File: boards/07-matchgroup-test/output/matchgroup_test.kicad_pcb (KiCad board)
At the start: 4 copper layers, 110 x 95 mm, 8 parts, among them J1 FFC6_MIPI, J2 HDMI19, J3 ADDR_HDR, U1 QFN48_DDR_CTRL, U2 QFN48_DRAM, U3 QFN24_MIPI, U4 BGA49_HDMI, U5 QFP48_SRAM

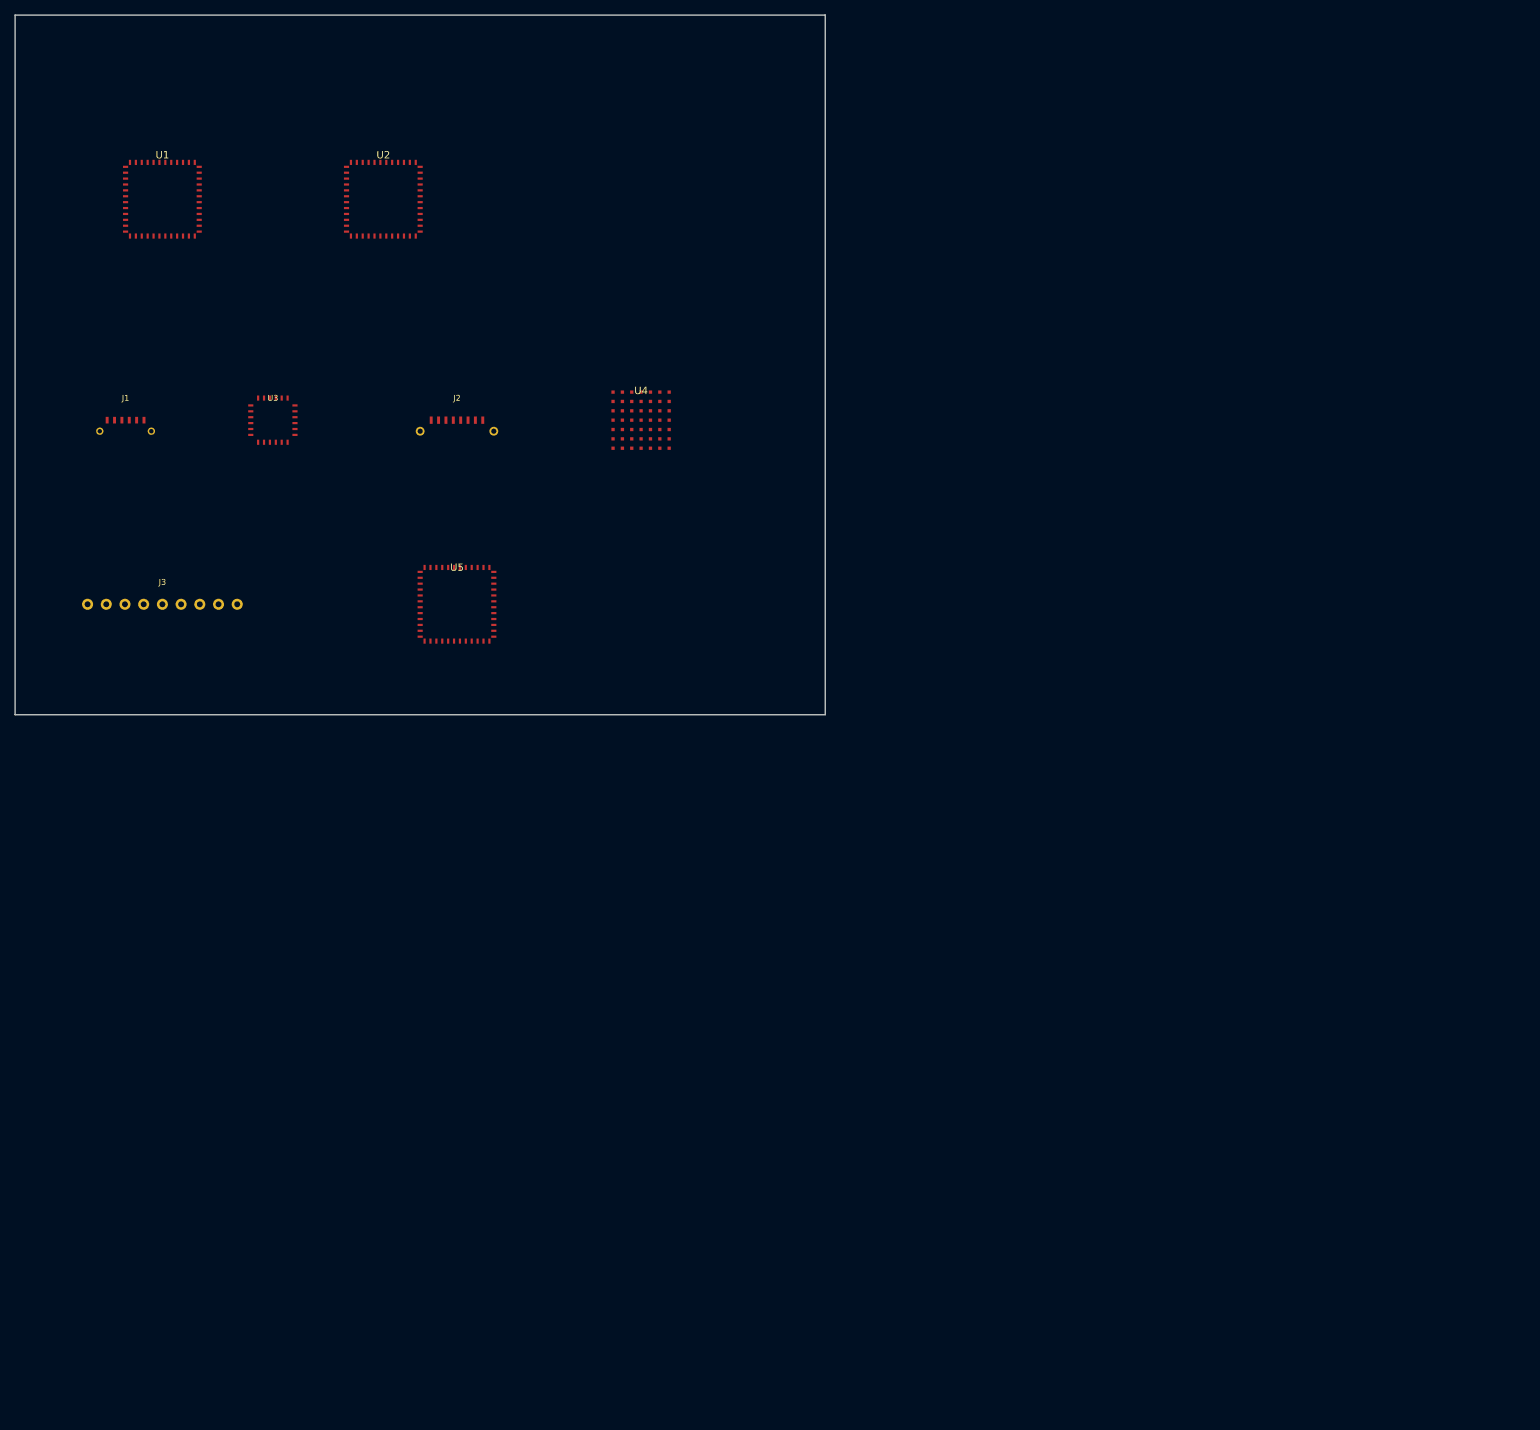
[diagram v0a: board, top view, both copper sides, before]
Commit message: fix(pcb): page-fit routed boards only; revert unrouted sources (refs #3714)
page_fit was applied to and committed for the UNROUTED board sources too.
Because the autorouter is absolute-grid-position-dependent, translating the
unrouted boards changed routing outcomes and turned CI red on three jobs:
- Test: board-02 re-route produced a platform-specific segment count.
- Diff-Pair (06) / Match-Group (07): re-routing the moved unrouted boards
  fractured plane nets under the copper-union pour audit (#3509/#3617).

page_fit is a pure post-route translation, so it must touch the ROUTED
output only:
- Revert every unrouted boards/*/output/<name>.kicad_pcb to origin/main
  (byte-identical); keep the page-fitted *_routed.kicad_pcb (gallery/viewer).
- Revert tests/router/test_board02_manufacturable_baseline.py to main
  (unrouted board-02 unchanged -> reproduces main's result).
- Build hook: _run_step_page_fit now operates on the routed PCB only and
  skips cleanly when no routed output exists, instead of falling back to and
  persisting a page-fit unrouted PCB.

Retains the sound geometry fixes (translation-invariant
point_to_segment_distance, _format_coord_mm, diffpair +1e-6 window tolerance).

Co-Authored-By: Claude Opus 4.7 <noreply@anthropic.com>
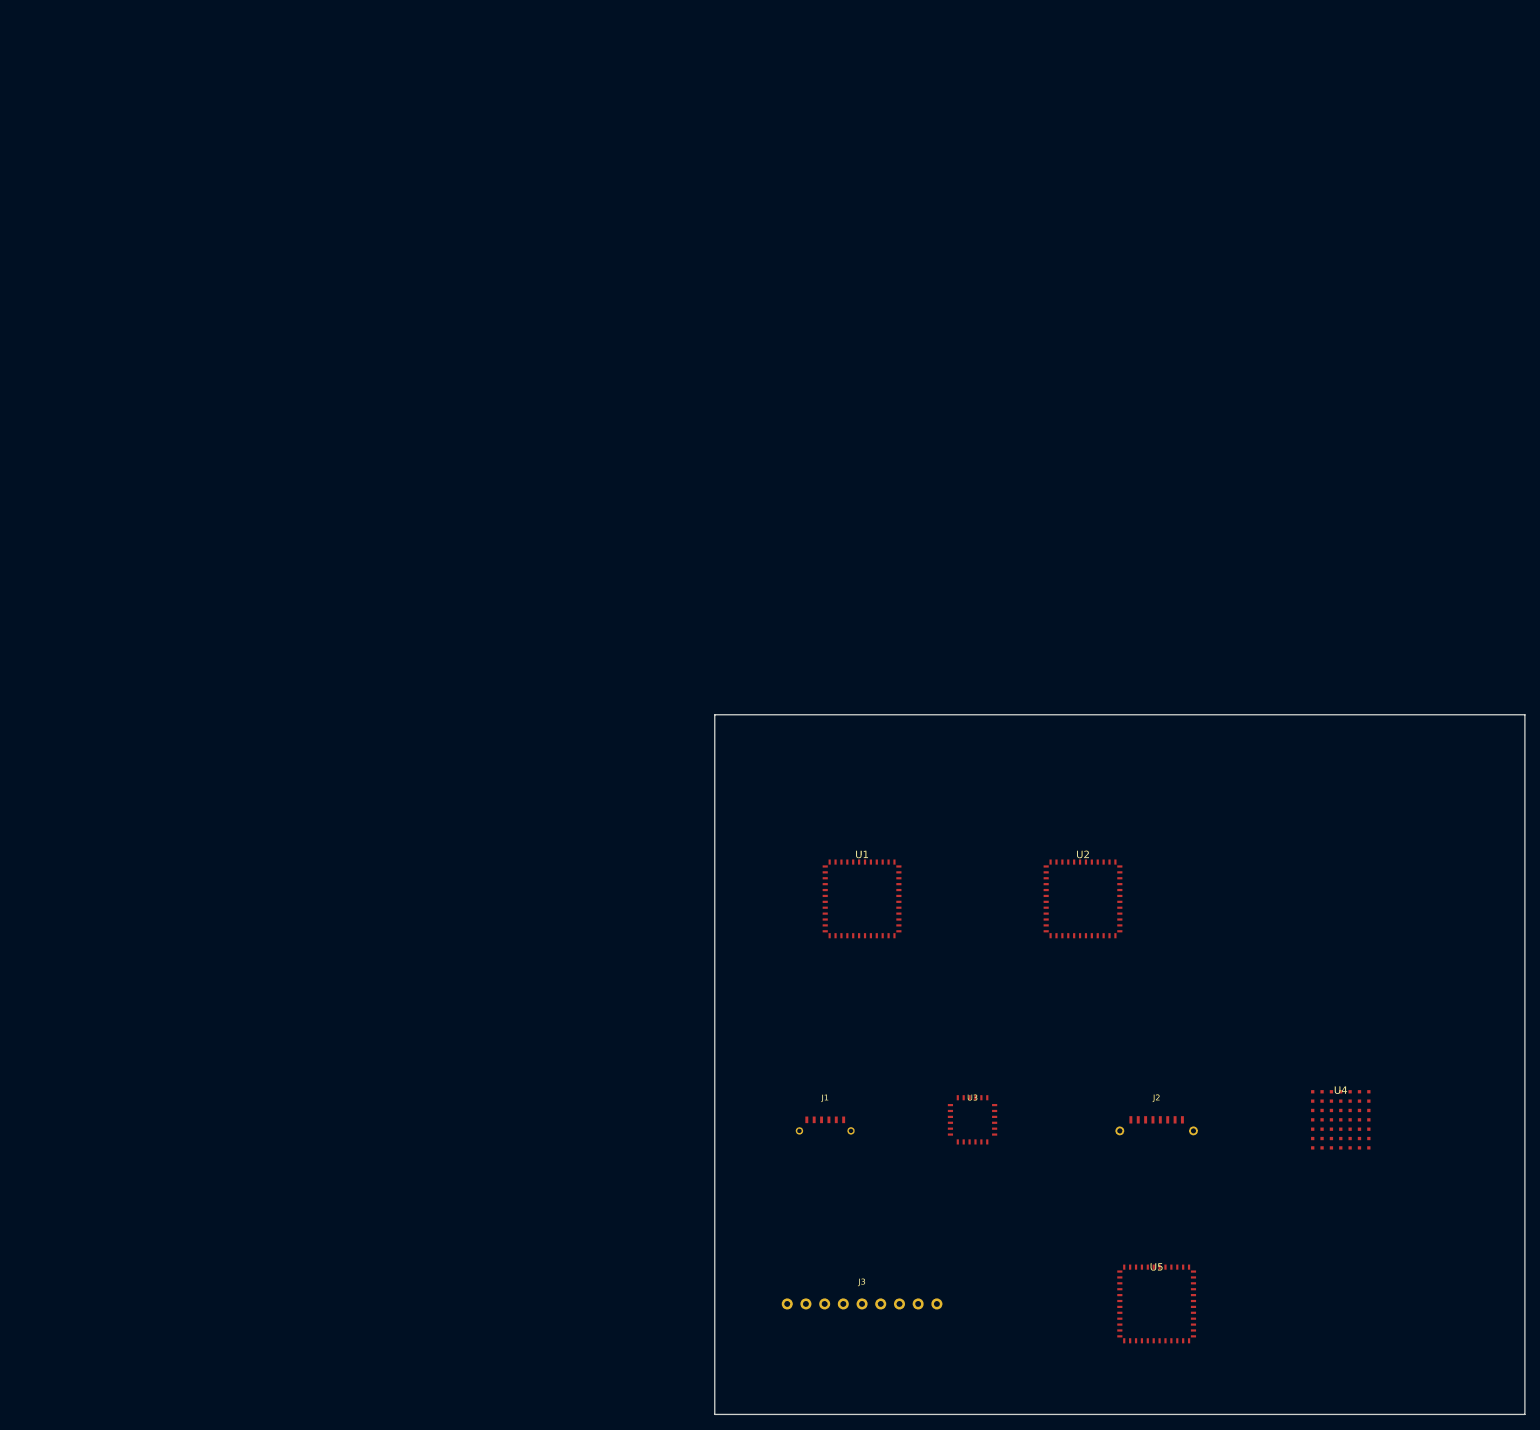
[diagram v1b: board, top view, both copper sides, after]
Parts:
- moved J1 134.4 mm to (115.0, 155.0)
- moved J2 134.4 mm to (160.0, 155.0)
- moved J3 134.4 mm to (120.0, 180.0)
- moved U1 134.4 mm to (120.0, 125.0)
- moved U2 134.4 mm to (150.0, 125.0)
- moved U3 134.4 mm to (135.0, 155.0)
- moved U4 134.4 mm to (185.0, 155.0)
- moved U5 134.4 mm to (160.0, 180.0)
